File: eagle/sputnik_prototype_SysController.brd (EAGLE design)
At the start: 100 x 80 mm, 70 parts, among them U1 MEGA128-A, X1 CRYSTAL-ABRACON-ABM3-SMD

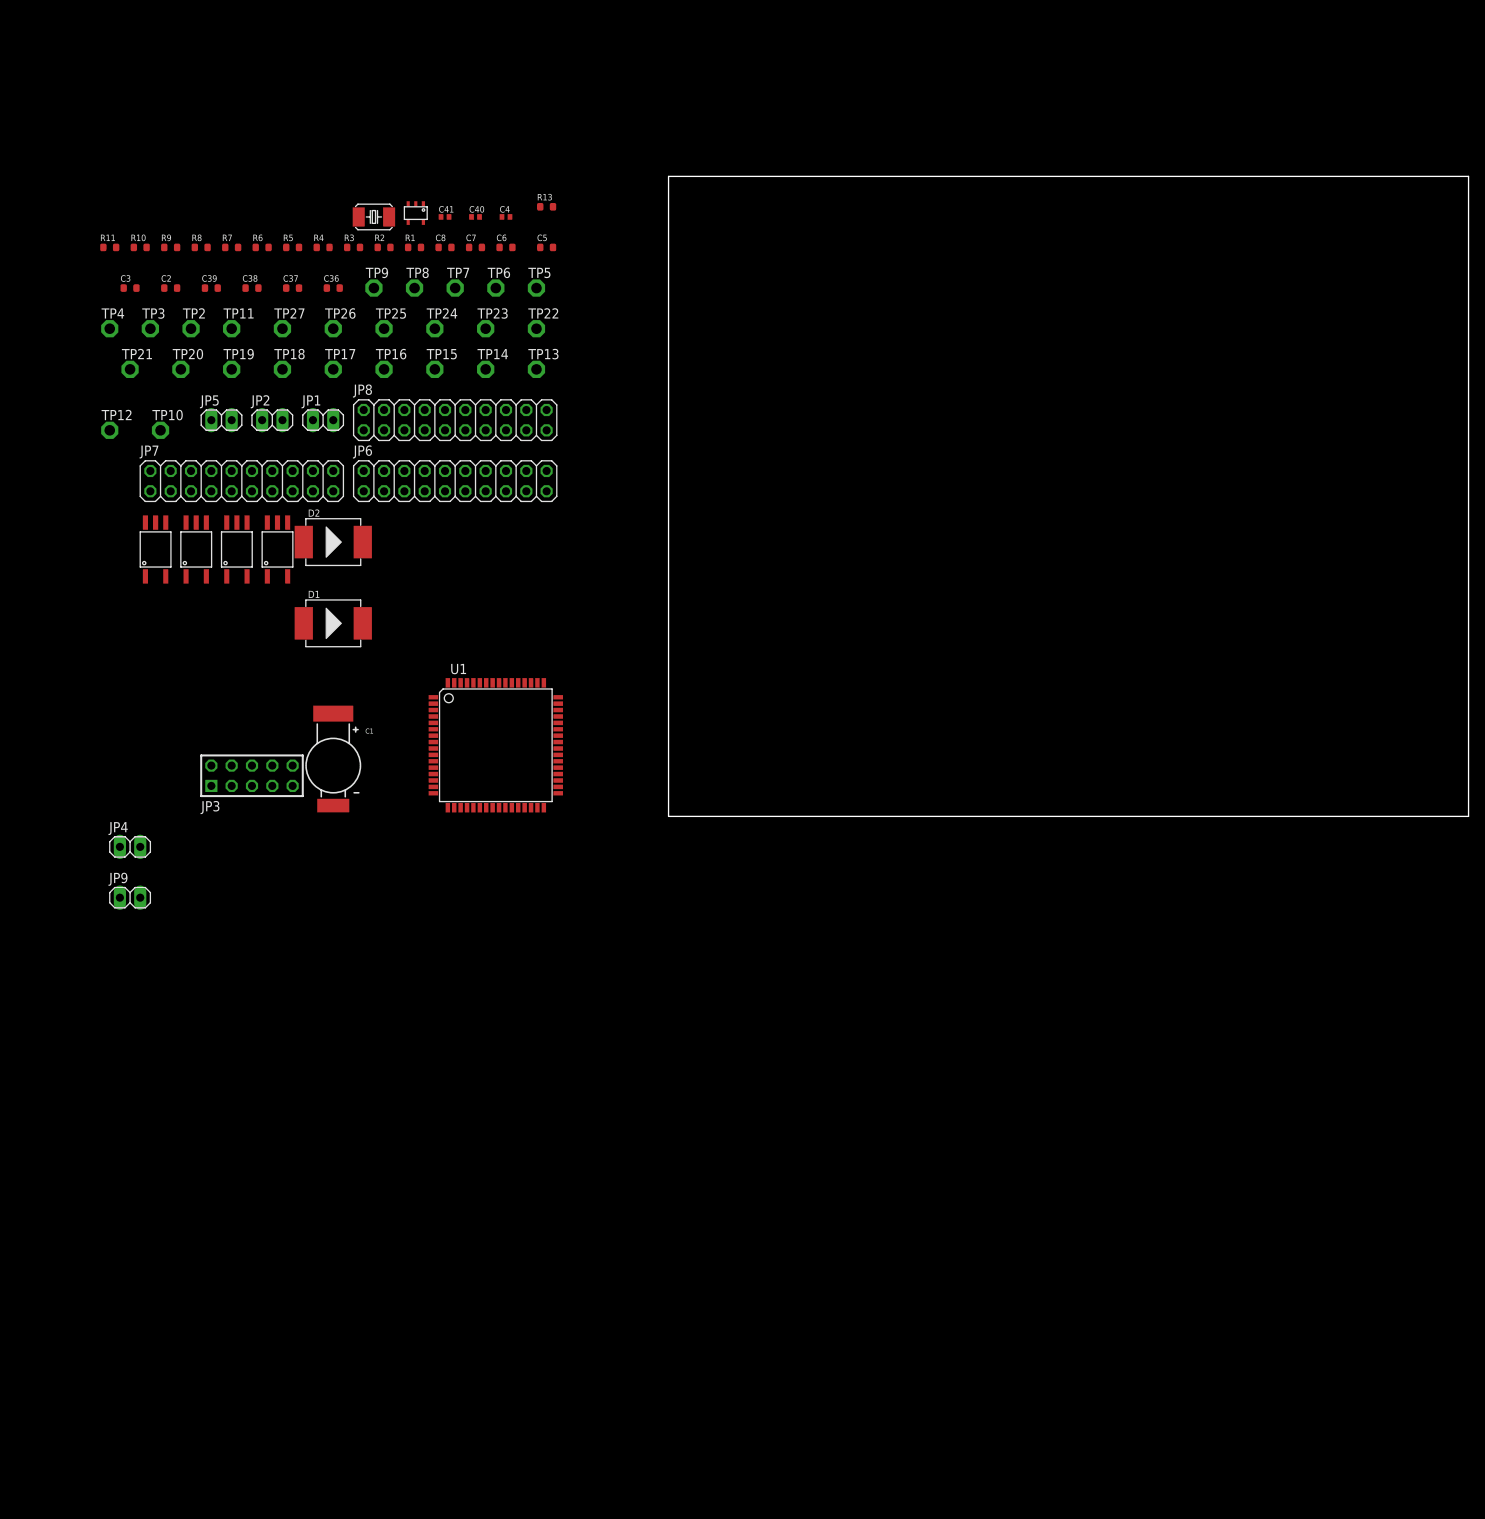
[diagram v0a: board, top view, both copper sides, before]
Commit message: Clean up on system controller board. Added 40 pin connector, board outline, ground planes. Killed all old spurious signals. Removed unecessary connectors. Still need to find small power controllers to sequence power to other boards.
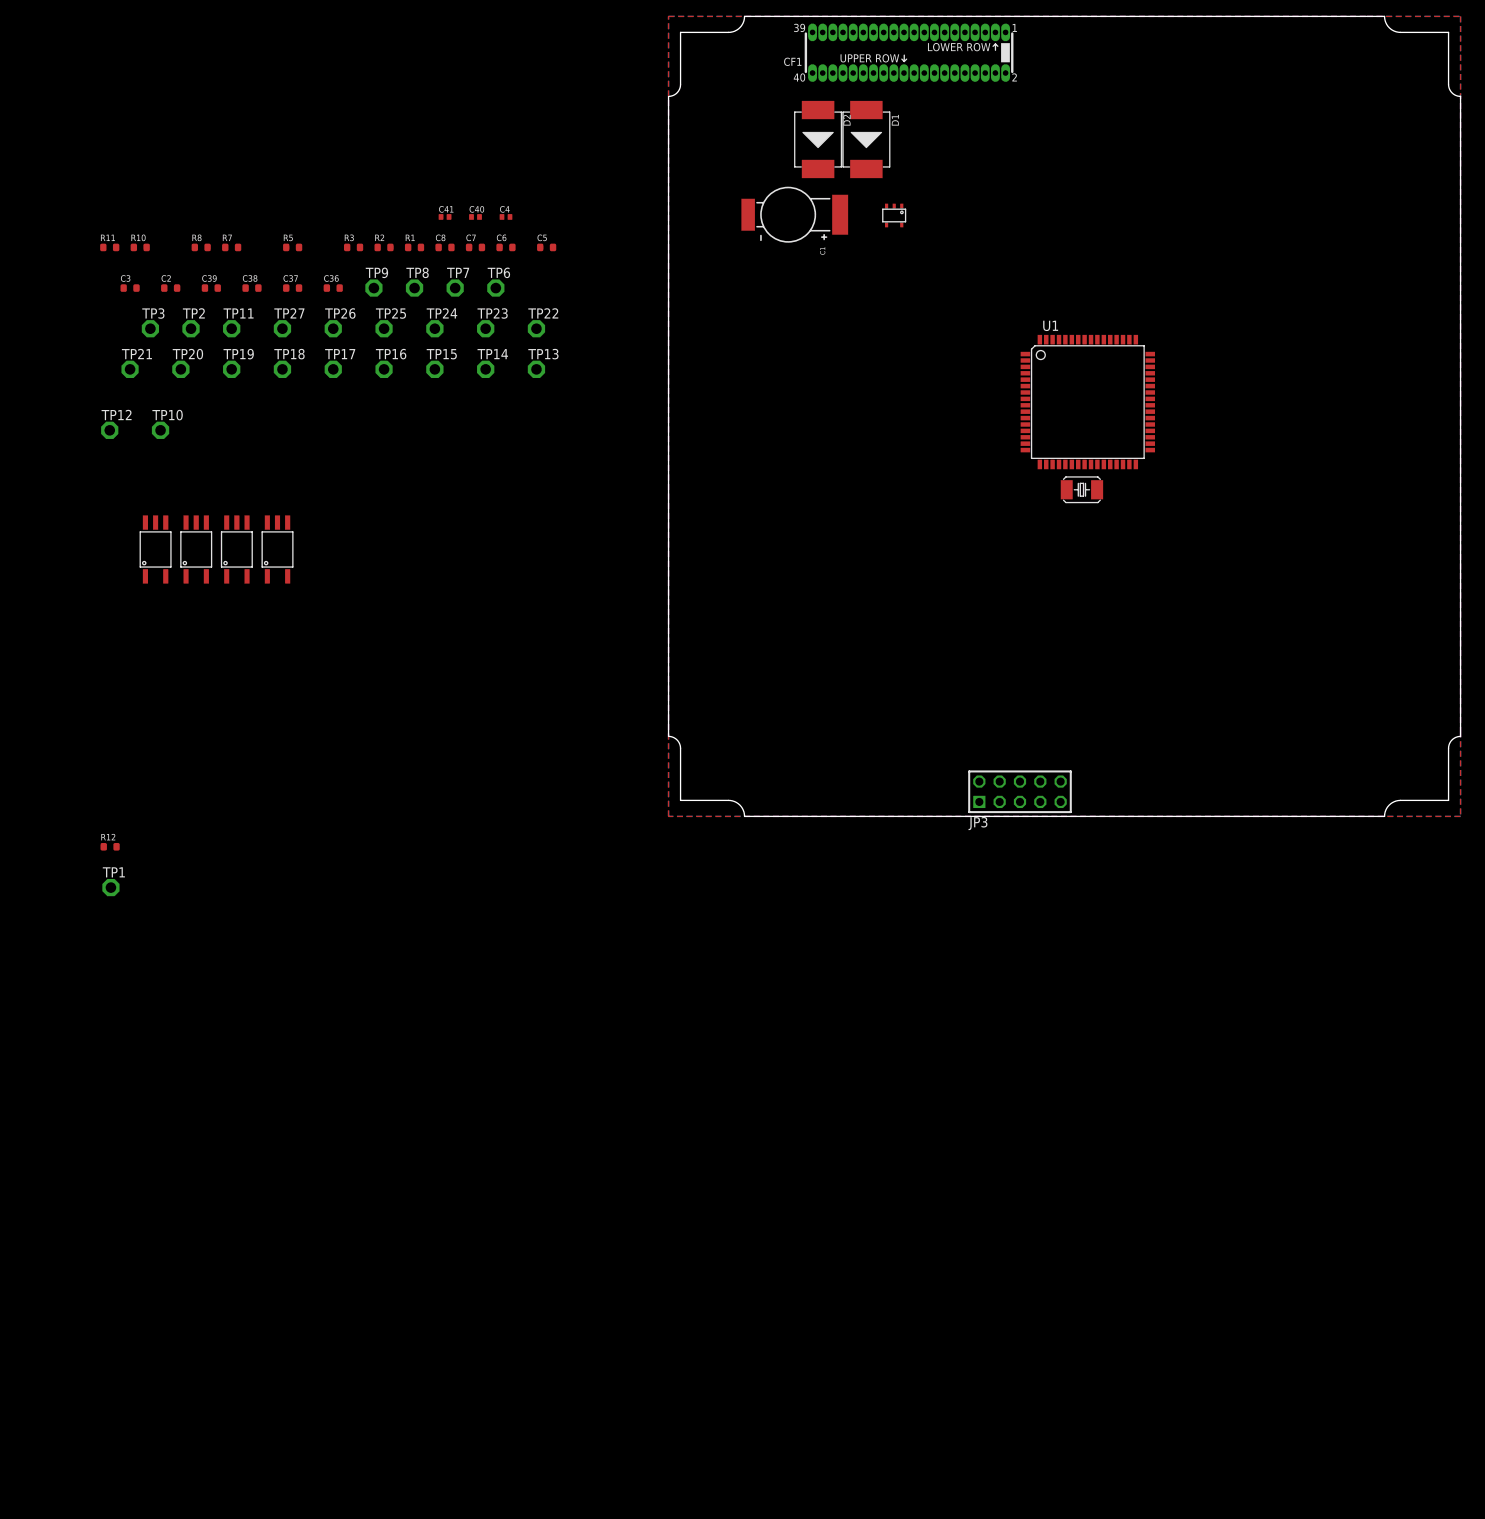
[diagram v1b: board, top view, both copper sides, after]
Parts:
- removed JP1, JP2, JP4, JP5, JP9: (no value), psas_c3_team05:1X02
- removed JP6, JP7, JP8: (no value), psas_c3_team05:2X10
- removed R13, R4, R6, R9: 390, rcl_custom:.0603-B-NOSILK
- removed TP4, TP5: TPSPAD1-13, testpad:P1-13
- added CF1: ORESAT-CONNECTOR-40PIN, oresat-eagle:HARWIN-ARCHER-M50-3202045
- added R12: 10k, rcl_custom:.0603-B-NOSILK
- added TP1: TPSPAD1-13, testpad:P1-13
- added U$5: (no value), oresat-eagle:ORESAT-CARD-V0.3
- moved JP3 96.0 mm to (43.9, 3.08)
- moved X1 94.8 mm to (51.7, 40.8)
- moved D1 90.0 mm to (24.7, 84.6), turned to 270 degrees
- moved C1 89.3 mm to (14.9, 75.2), turned to 270 degrees
- moved U1 85.5 mm to (52.4, 51.8)
- moved D2 78.8 mm to (18.7, 84.6), turned to 270 degrees
- moved U$8 59.8 mm to (26.8, 75.9)
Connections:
- removed net N$2: C36.2, C37.2, C38.2, C39.2, C4.1, JP3.4, JP3.7, U$8.5, U1.21, U1.52, U1.62, U1.64
- removed net N$21: R9.1, U$4.2
- removed net N$25: D1.1, JP4.1
- removed net N$26: D2.1, JP9.1
- removed net N$3: R13.1, U$3.2
- removed net N$7: R4.1, U$1.2
- removed net N$9: R6.1
- removed net PTA1/UART0_RX: R1.1
- removed net PTA2/UART1_TX: R10.1
- removed net PTA20/RESET: U1.5
- removed net UART1_RX: JP5.1, R2.1, TP4.TP
- removed net UART1_TX: JP5.2, R5.1, TP5.TP
- new net +3V3: C2.2, C3.2, C36.2, C37.2, C38.2, C39.2, C4.1, JP3.4, JP3.7, U$2.5, U$4.5, U$8.5, U1.21, U1.52, U1.62, U1.64
- new net FC_UART_RX: CF1.P$19, CF1.P$20, R2.1
- new net FC_UART_TX: CF1.P$21, CF1.P$22, R5.1
- new net FC_UART_VCC: C5.2, CF1.P$17, CF1.P$18, U$1.5
- new net LGR_UART_RX: CF1.P$25, CF1.P$26, R1.1
- new net LGR_UART_TX: CF1.P$27, CF1.P$28, R10.1
- new net LGR_UART_VCC: C6.2, CF1.P$23, CF1.P$24, U$3.5
- new net N$22: R12.2, TP1.TP, U$8.3
- new net VBUS: CF1.P$29, CF1.P$30, CF1.P$31, CF1.P$32, D1.1
- new net VSOL: CF1.P$33, CF1.P$34, CF1.P$35, CF1.P$36, D2.1
- net GND: now also CF1.P$37, CF1.P$38, CF1.P$39, CF1.P$40, U$1.2, U$3.2, U$4.2; no longer JP1.2, JP4.2, JP6.19, JP6.20, JP7.19, JP7.20, JP8.19, JP8.20, JP9.2, R13.2, R4.2, R6.2, R9.2
- net N$36: now also R12.1; no longer C1.+
- net PA0: no longer JP6.17, JP6.18
- net PA1: no longer JP6.15, JP6.16
- net PA2: no longer JP6.13, JP6.14
- net PA3: no longer JP6.11, JP6.12
- net PA4: no longer JP6.10, JP6.9
- net PA5: no longer JP6.7, JP6.8
- net PA6: no longer JP6.5, JP6.6
- net PA7: no longer JP6.3, JP6.4
- net PB0: no longer JP7.17, JP7.18
- net PB1: no longer JP7.15, JP7.16
- net PB2: no longer JP7.13, JP7.14
- net PB3: no longer JP7.11, JP7.12
- net PB4: no longer JP7.10, JP7.9
- net PB5: no longer JP7.7, JP7.8
- net PB6: no longer JP7.5, JP7.6
- net PB7: no longer JP7.3, JP7.4
- net PC0: no longer JP8.17, JP8.18
- net PC1: no longer JP8.15, JP8.16
- net PC2: no longer JP8.13, JP8.14
- net PC3: no longer JP8.11, JP8.12
- net PC4: no longer JP8.10, JP8.9
- net PC5: no longer JP8.7, JP8.8
- net PC6: no longer JP8.5, JP8.6
- net PC7: no longer JP8.3, JP8.4
- net SDA: now also CF1.P$15, CF1.P$16; no longer JP2.2
- net SDL: now also CF1.P$13, CF1.P$14; no longer JP2.1
- net V+: now also C1.+; no longer C2.2, C3.2, C5.2, C6.2, JP1.1, JP6.1, JP6.2, JP7.1, JP7.2, JP8.1, JP8.2, U$1.5, U$2.5, U$3.5, U$4.5
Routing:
- added copper zone on layer 1, net GND
- added copper zone on layer 15, net GND
- added copper zone on layer 16, net GND
- added copper zone on layer 2, net GND
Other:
- board size 100 x 80 mm -> 99 x 100 mm

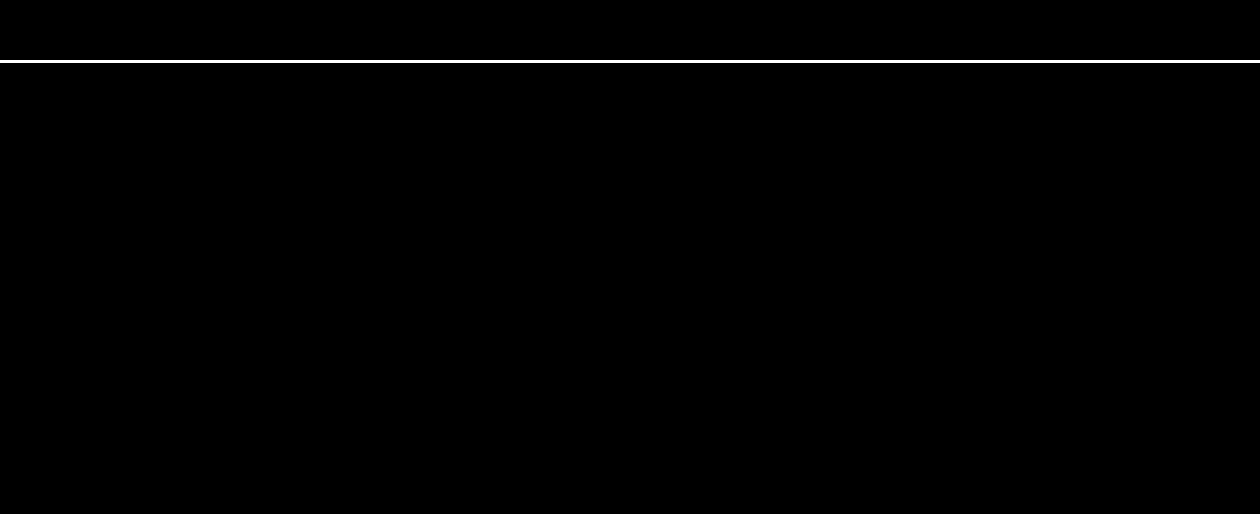
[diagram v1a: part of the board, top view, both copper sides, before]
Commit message: Newest outline of SC board, added secondary connector because we're going to need it for the output.
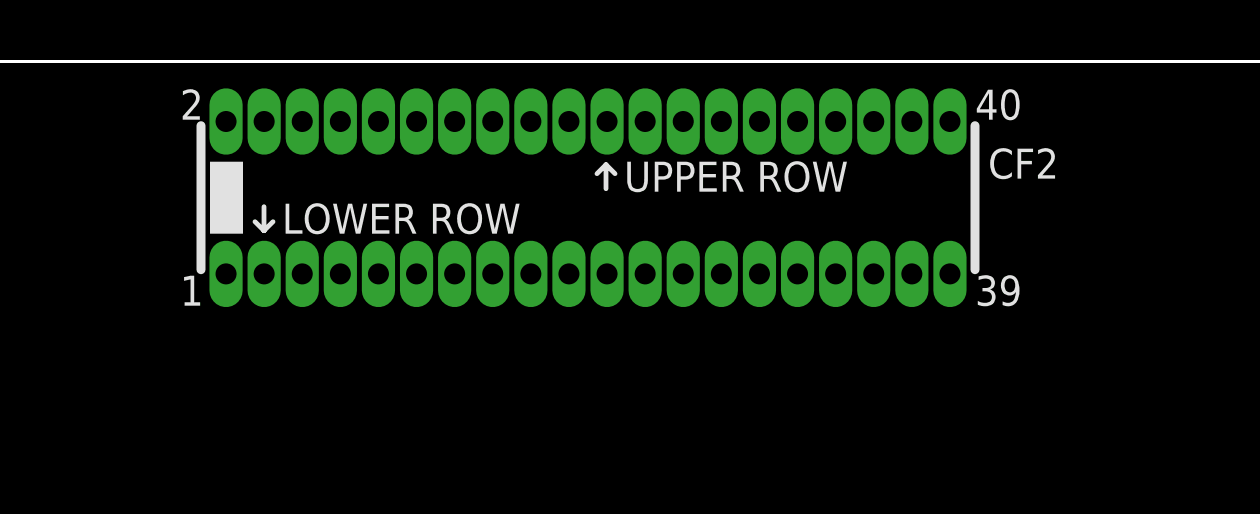
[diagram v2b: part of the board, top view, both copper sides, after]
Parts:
- added CF2: ORESAT-CONNECTOR-40PIN, oresat-eagle:HARWIN-ARCHER-M50-3202045
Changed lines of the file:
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@@
 <setting verticaltext="up"/>
 </settings>
-<grid distance="0.1" unitdist="mm" unit="mm" style="lines" multiple="1" display="yes" altdistance="0.025" altunitdist="inch" altunit="inch"/>
+<grid distance="1" unitdist="mm" unit="mm" style="lines" multiple="1" display="yes" altdistance="0.025" altunitdist="inch" altunit="inch"/>
 <layers>
 <layer number="1" name="Top" color="4" fill="1" visible="yes" active="yes"/>
@@
 <layer number="37" name="tTest" color="7" fill="1" visible="no" active="yes"/>
 <layer number="38" name="bTest" color="7" fill="1" visible="no" active="yes"/>
-<layer number="39" name="tKeepout" color="4" fill="11" visible="no" active="yes"/>
-<layer number="40" name="bKeepout" color="1" fill="11" visible="no" active="yes"/>
+<layer number="39" name="tKeepout" color="4" fill="11" visible="yes" active="yes"/>
+<layer number="40" name="bKeepout" color="1" fill="11" visible="yes" active="yes"/>
 <layer number="41" name="tRestrict" color="4" fill="10" visible="no" active="yes"/>
 <layer number="42" name="bRestrict" color="1" fill="10" visible="no" active="yes"/>
@@
 <element name="X1" library="crystal-abracon-abm3-smd" package="CRYSTAL-ABRACON-ABM3-SMD" value="CRYSTAL-ABRACON-ABM3-SMD" x="51.67" y="40.83"/>
 <element name="CF1" library="oresat-eagle" package="HARWIN-ARCHER-M50-3202045" value="ORESAT-CONNECTOR-40PIN" x="30.065" y="95.46" locked="yes" rot="R180"/>
-<element name="U$5" library="oresat-eagle" package="ORESAT-CARD-V0.3" value="" x="0" y="0" locked="yes"/>
 <element name="R12" library="rcl_custom" package=".0603-B-NOSILK" value="10k" x="-69.8" y="-3.8"/>
 <element name="TP1" library="testpad" package="P1-13" value="TPSPAD1-13" x="-69.7" y="-8.9">
 <attribute name="TP_SIGNAL_NAME" value="" x="-69.7" y="-8.9" size="1.778" layer="27" display="off"/>
 </element>
+<element name="U$5" library="oresat-eagle" package="ORESAT-CARD-V0.3" value="" x="0" y="0" locked="yes"/>
+<element name="CF2" library="oresat-eagle" package="HARWIN-ARCHER-M50-3202045" value="ORESAT-CONNECTOR-40PIN" x="65.065" y="95.46" locked="yes"/>
 </elements>
 <signals>
